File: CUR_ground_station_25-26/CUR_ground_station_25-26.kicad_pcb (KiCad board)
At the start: 4 copper layers, 74 x 51 mm, 82 parts, among them J1 Conn_01x02, J2 UJ20-C-H-G-SMT-P16-TR, J3 Conn_Coaxial_Small, J4 Conn_01x04_Pin, Q1 NTR4003N, Q2 NTR4003N, SW1 PTS815SJM250SMTRLFS, SW2 PTS815SJM250SMTRLFS, SW3 PTS815SJM250SMTRLFS, SW4 PTS815SJM250SMTRLFS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

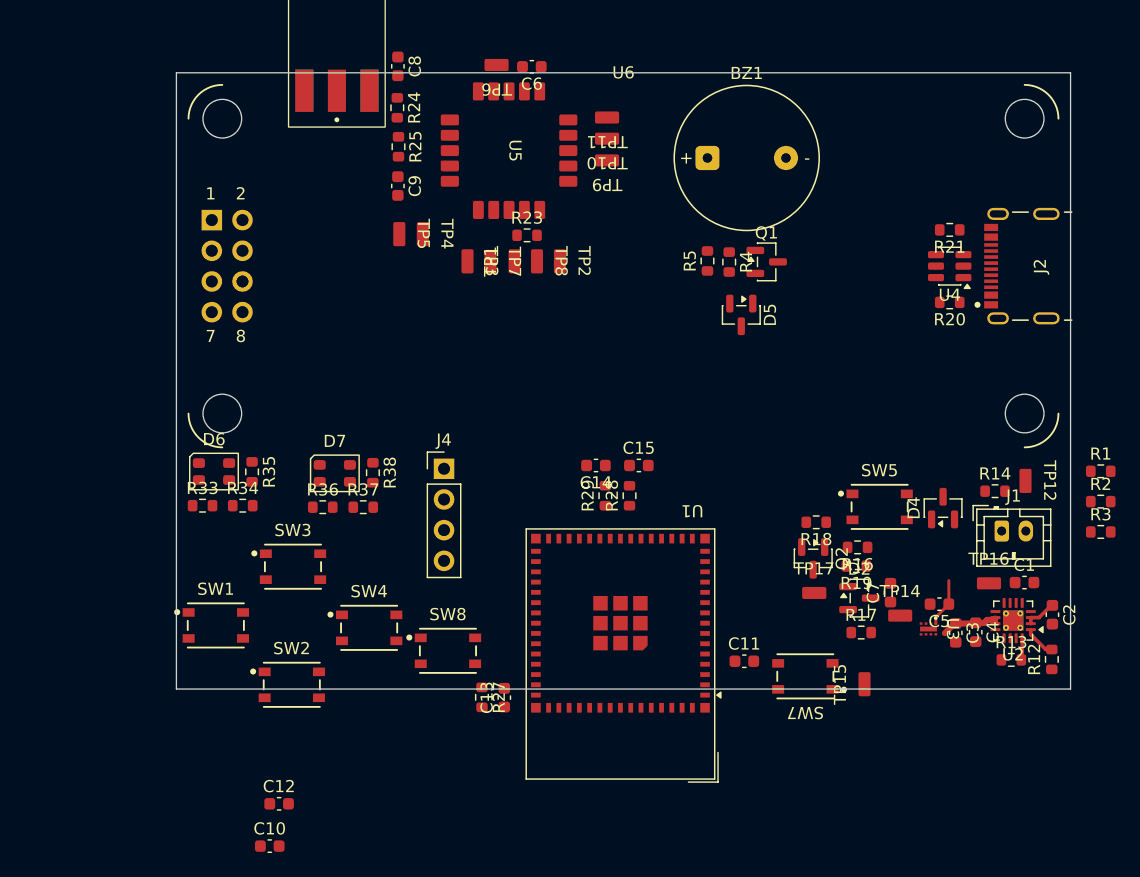
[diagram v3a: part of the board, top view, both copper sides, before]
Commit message: Add mounting holes
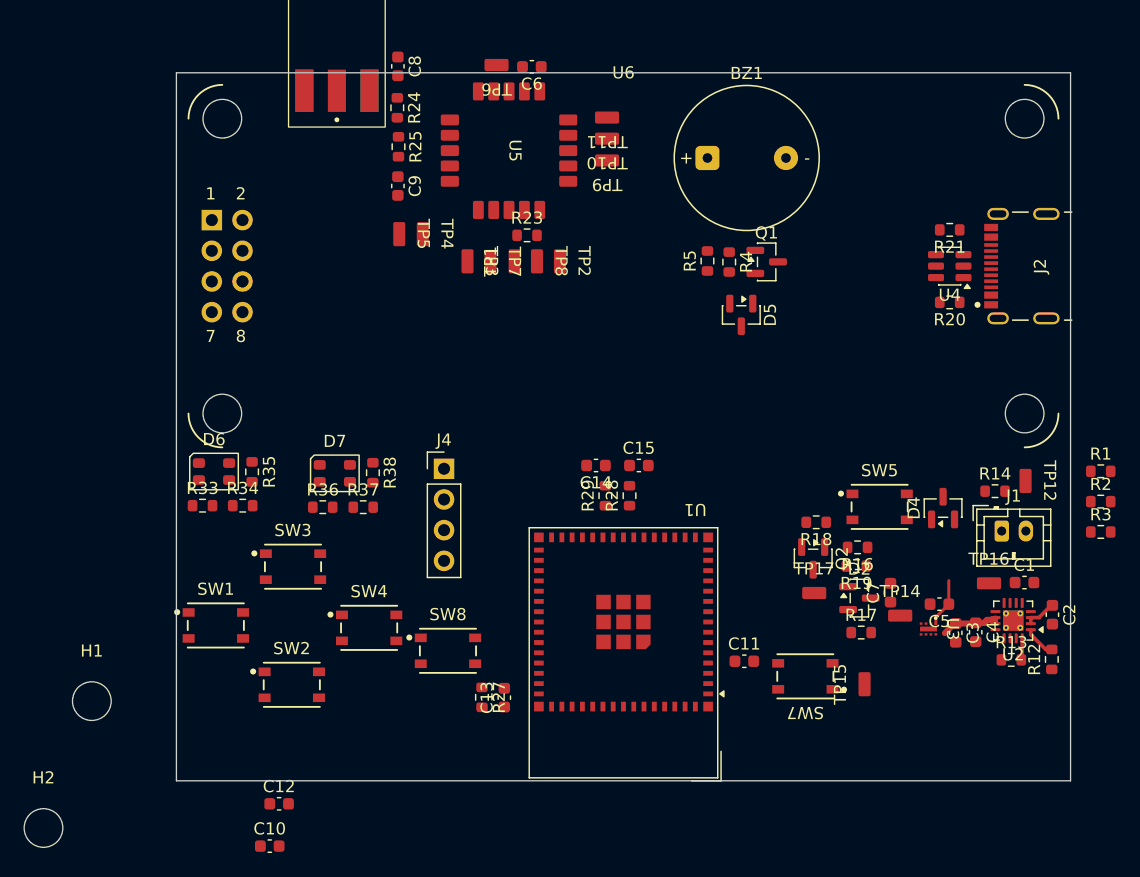
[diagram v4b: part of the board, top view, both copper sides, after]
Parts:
- added H1: MountingHole, MountingHole:MountingHole_3.2mm_M3, F.Cu at (41.5, 102.0)
- added H2: MountingHole, MountingHole:MountingHole_3.2mm_M3, F.Cu at (37.5, 112.5)
- moved U1 0.27 mm to (85.5, 98.0)
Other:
- board size 74 x 51 mm -> 74 x 58.6 mm
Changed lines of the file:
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@@
 		)
 	)
+	(footprint "MountingHole:MountingHole_3.2mm_M3"
+		(layer "F.Cu")
+		(at 37.5 112.5)
+		(descr "Mounting Hole 3.2mm, M3, no annular, generated by kicad-footprint-generator mountinghole.py")
+		(tags "mountinghole M3")
+		(property "Reference" "H2"
+			(at 0 -4.15 0)
+			(layer "F.SilkS")
+			(effects
+				(font
+					(size 1 1)
+					(thickness 0.15)
+				)
+			)
+		)
+		(property "Value" "MountingHole"
+			(at 0 4.15 0)
+			(layer "F.Fab")
+			(effects
+				(font
+					(size 1 1)
+					(thickness 0.15)
+				)
+			)
+		)
+		(property "Datasheet" "~"
+			(at 0 0 0)
+			(layer "F.Fab")
+			(hide yes)
+			(effects
+				(font
+					(size 1.27 1.27)
+					(thickness 0.15)
+				)
+			)
+		)
+		(property "Description" "Mounting Hole without connection"
+			(at 0 0 0)
+			(layer "F.Fab")
+			(hide yes)
+			(effects
+				(font
+					(size 1.27 1.27)
+					(thickness 0.15)
+				)
+			)
+		)
+		(property ki_fp_filters "MountingHole*")
+		(sheetname "/")
+		(sheetfile "CUR_ground_station_25-26.kicad_sch")
+		(attr exclude_from_pos_files exclude_from_bom)
+		(fp_circle
+			(center 0 0)
+			(end 3.2 0)
+			(stroke
+				(width 0.15)
+				(type solid)
+			)
+			(fill no)
+			(layer "Cmts.User")
+		)
+		(fp_circle
+			(center 0 0)
+			(end 3.45 0)
+			(stroke
+				(width 0.05)
+				(type solid)
+			)
+			(fill no)
+			(layer "F.CrtYd")
+		)
+		(fp_text user "${REFERENCE}"
+			(at 0 0 0)
+			(layer "F.Fab")
+			(effects
+				(font
+					(size 1 1)
+					(thickness 0.15)
+				)
+			)
+		)
+		(pad "" np_thru_hole circle
+			(at 0 0)
+			(size 3.2 3.2)
+			(drill 3.2)
+			(layers "*.Cu" "*.Mask")
+		)
+		(embedded_fonts no)
+	)
 	(footprint "Package_TO_SOT_SMD:SOT-23"
 		(layer "F.Cu")
@@
 		)
 	)
+	(footprint "MountingHole:MountingHole_3.2mm_M3"
+		(layer "F.Cu")
+		(at 41.5 102)
+		(descr "Mounting Hole 3.2mm, M3, no annular, generated by kicad-footprint-generator mountinghole.py")
+		(tags "mountinghole M3")
+		(property "Reference" "H1"
+			(at 0 -4.15 0)
+			(layer "F.SilkS")
+			(effects
+				(font
+					(size 1 1)
+					(thickness 0.15)
+				)
+			)
+		)
+		(property "Value" "MountingHole"
+			(at 0 4.15 0)
+			(layer "F.Fab")
+			(effects
+				(font
+					(size 1 1)
+					(thickness 0.15)
+				)
+			)
+		)
+		(property "Datasheet" "~"
+			(at 0 0 0)
+			(layer "F.Fab")
+			(hide yes)
+			(effects
+				(font
+					(size 1.27 1.27)
+					(thickness 0.15)
+				)
+			)
+		)
+		(property "Description" "Mounting Hole without connection"
+			(at 0 0 0)
+			(layer "F.Fab")
+			(hide yes)
+			(effects
+				(font
+					(size 1.27 1.27)
+					(thickness 0.15)
+				)
+			)
+		)
+		(property ki_fp_filters "MountingHole*")
+		(sheetname "/")
+		(sheetfile "CUR_ground_station_25-26.kicad_sch")
+		(attr exclude_from_pos_files exclude_from_bom)
+		(fp_circle
+			(center 0 0)
+			(end 3.2 0)
+			(stroke
+				(width 0.15)
+				(type solid)
+			)
+			(fill no)
+			(layer "Cmts.User")
+		)
+		(fp_circle
+			(center 0 0)
+			(end 3.45 0)
+			(stroke
+				(width 0.05)
+				(type solid)
+			)
+			(fill no)
+			(layer "F.CrtYd")
+		)
+		(fp_text user "${REFERENCE}"
+			(at 0 0 0)
+			(layer "F.Fab")
+			(effects
+				(font
+					(size 1 1)
+					(thickness 0.15)
+				)
+			)
+		)
+		(pad "" np_thru_hole circle
+			(at 0 0)
+			(size 3.2 3.2)
+			(drill 3.2)
+			(layers "*.Cu" "*.Mask")
+		)
+		(embedded_fonts no)
+	)
 	(footprint "Resistor_SMD:R_0603_1608Metric"
 		(layer "F.Cu")
@@
 	(footprint "RF_Module:ESP32-S2-MINI-1"
 		(layer "F.Cu")
-		(at 85.25 98.1 180)
+		(at 85.5 98 180)
 		(descr "2.4 GHz Wi-Fi and Bluetooth combo chip, external antenna, https://www.espressif.com/sites/default/files/documentation/esp32-s3-mini-1_mini-1u_datasheet_en.pdf")
 		(tags "2.4 GHz Wi-Fi Bluetooth external antenna espressif  20*15.4mm")
@@
 			(polygon
 				(pts
-					(xy 62.55 103.35) (xy 107.95 103.35) (xy 107.95 122.85) (xy 62.55 122.85)
+					(xy 62.8 103.25) (xy 108.2 103.25) (xy 108.2 122.75) (xy 62.8 122.75)
 				)
 			)
@@
 	(gr_rect
 		(start 48.5 50)
-		(end 122.5 101)
+		(end 122.5 108.595342)
 		(stroke
 			(width 0.05)

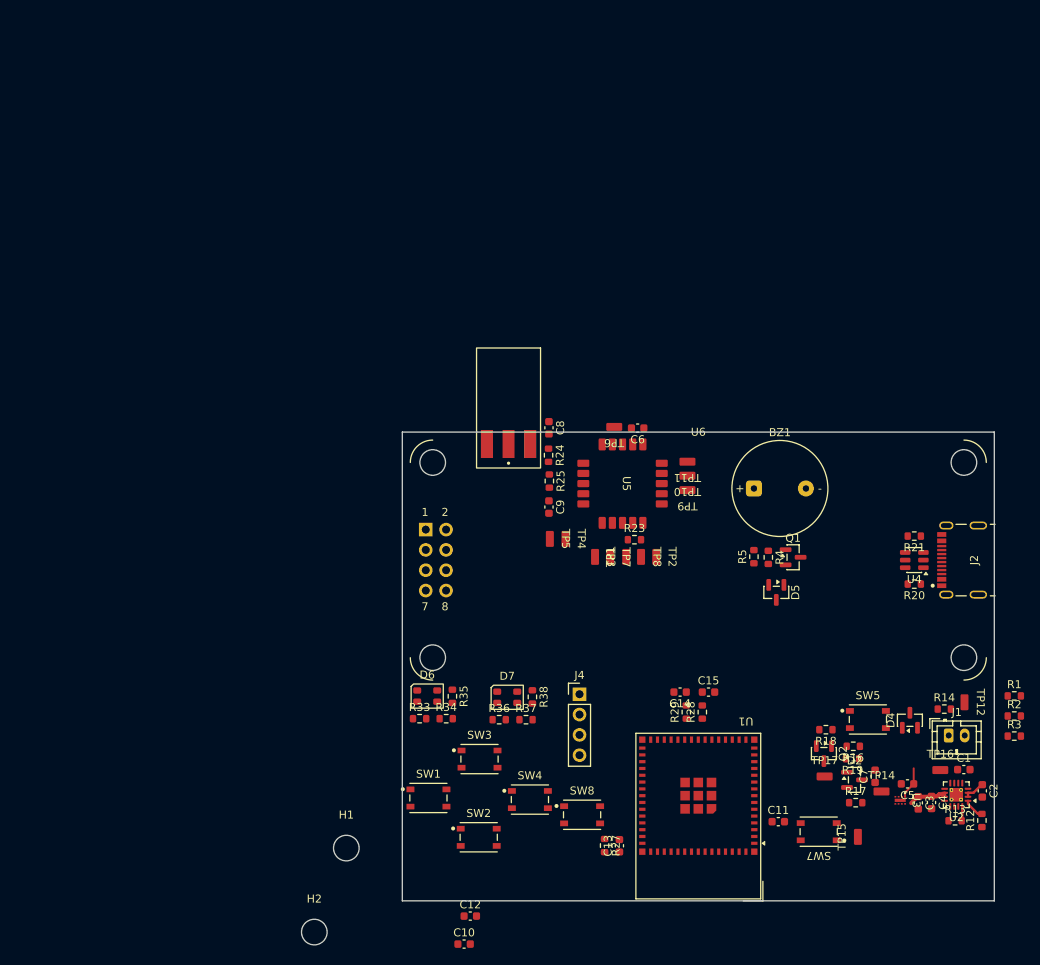
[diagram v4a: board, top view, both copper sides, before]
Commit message: switched battery connector, put mounting holes in place
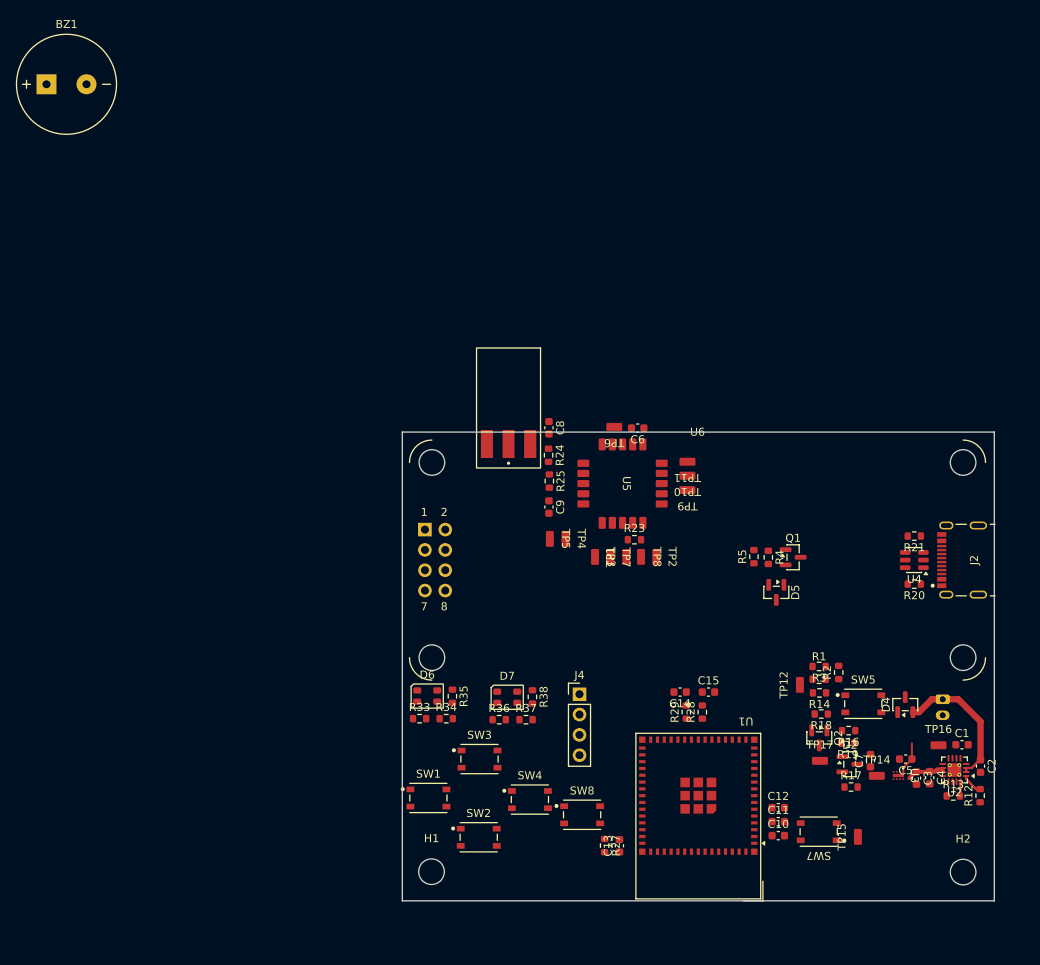
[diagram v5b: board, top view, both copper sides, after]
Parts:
- BZ1: footprint Buzzer_SameSky:Buzzer_SameSky_CEM-1203_42 -> Buzzer_SameSky:Buzzer_SameSky_CPT-1207-3TH
- J1: footprint Connector_JST:JST_PH_B2B-PH-K_1x02_P2.00mm_Vertical -> Connector_JST:JST_PH_S2B-PH-K_1x02_P2.00mm_Horizontal; moved to B.Cu
- moved BZ1 102.5 mm to (6.53, 6.53)
- moved H2 81.4 mm to (118.6, 105.0)
- moved C10 41.5 mm to (95.5, 100.5)
- moved C12 40.8 mm to (95.5, 97.0)
- moved R3 25.9 mm to (100.6, 79.3), turned to 180 degrees
- moved R1 24.5 mm to (100.6, 80.9)
- moved R2 22.6 mm to (103.0, 80.0), turned to 90 degrees
- moved TP12 20.7 mm to (98.2, 81.6), turned to 90 degrees
- moved R14 15.7 mm to (100.7, 82.6), turned to 180 degrees
- moved H1 11.1 mm to (52.1, 105.0)
- moved J1 4.59 mm to (116.0, 83.4), turned to -90 degrees
- moved C1 3.11 mm to (118.5, 89.1)
- moved R13 3.11 mm to (117.4, 95.5)
- moved C2 3.11 mm to (120.8, 91.7)
- moved C3 3.11 mm to (112.8, 93.2)
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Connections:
- U1 pad 7: /MCU/BATT_VSENSE -> /MCU/PWR_BTN
- U1 pad 9: /MCU/PWR_BTN -> /MCU/BATT_VSENSE
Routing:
- net +BATT: track 2.78 -> 17.8 mm

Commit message: Started routing power
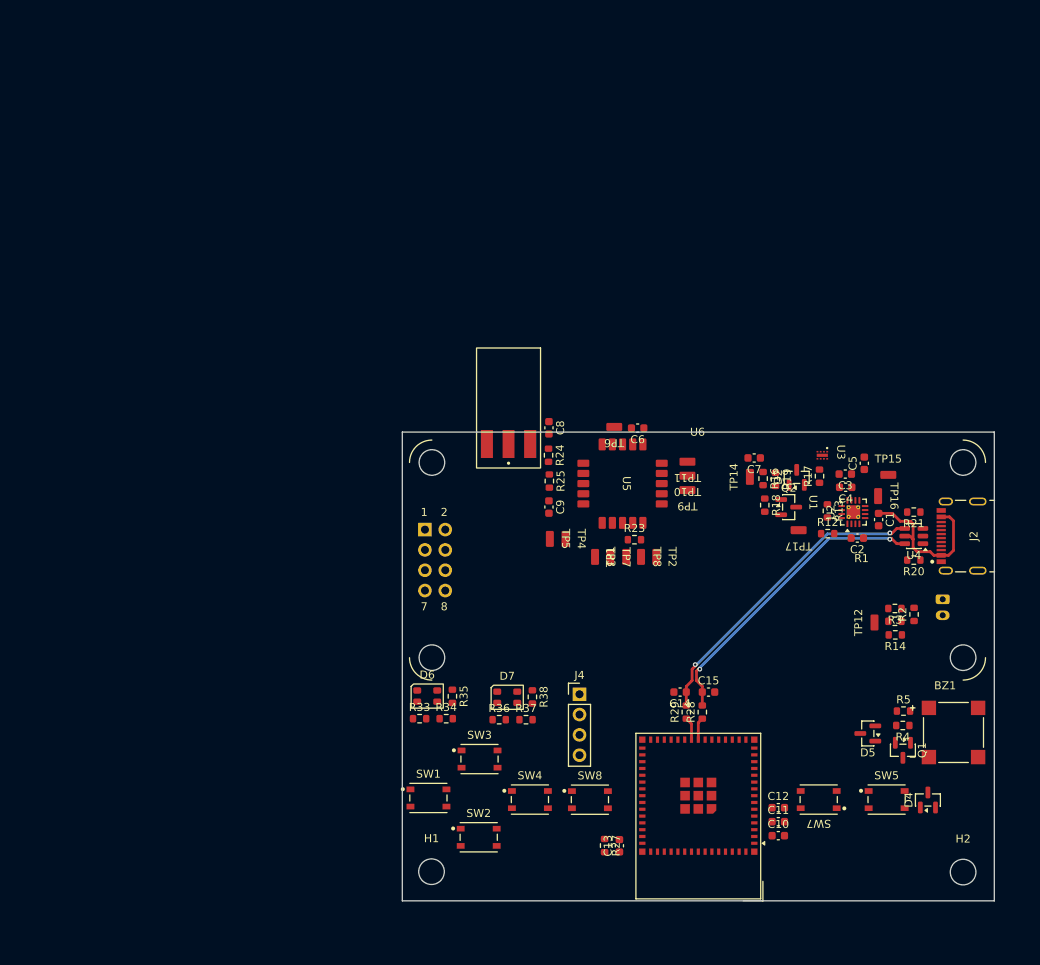
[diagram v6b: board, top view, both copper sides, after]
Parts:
- BZ1: footprint Buzzer_SameSky:Buzzer_SameSky_CPT-1207-3TH -> Buzzer_SameSky:XDCR_CMT-7525-03-SMT-TR
- moved BZ1 137.3 mm to (117.4, 87.5)
- moved TP15 45.4 mm to (109.3, 55.4), turned to 0 degrees
- moved U3 41.1 mm to (101.0, 52.9)
- moved TP14 40.6 mm to (92.0, 55.6), turned to 90 degrees
- moved C7 40.5 mm to (92.5, 53.2), turned to 180 degrees
- moved R17 39.1 mm to (100.6, 55.5), turned to 90 degrees
- moved C3 39.0 mm to (103.9, 55.2), turned to 180 degrees
- moved R13 39.0 mm to (101.6, 59.8), turned to -90 degrees
- moved R12 37.9 mm to (101.7, 62.7), turned to 0 degrees
- moved C4 37.8 mm to (103.9, 56.9), turned to 180 degrees
- moved C5 37.3 mm to (106.2, 53.9), turned to 90 degrees
- moved D2 36.5 mm to (97.8, 55.7), turned to 90 degrees
- moved U2 34.6 mm to (104.9, 60.0), turned to 90 degrees
- moved R19 34.2 mm to (95.1, 55.9), turned to -90 degrees
- moved R16 33.3 mm to (93.6, 55.8), turned to -90 degrees
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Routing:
- net /MCU/USB_D+: track 0.00 -> 38.9 mm, vias 0 -> 2
- net /MCU/USB_D-: track 0.00 -> 38.0 mm, vias 0 -> 2
- net VBUS: track 0.00 -> 20.2 mm
- net +BATT: track 17.8 -> 0.17 mm
- net IN: track 4.98 -> 0.17 mm
- net +3V3: track 4.01 -> 0.00 mm
- net Net-(U1-USB_D+): track 0.00 -> 2.89 mm
- net Net-(U1-USB_D-): track 0.00 -> 2.83 mm
- net Net-(U2-TS): track 2.65 -> 0.00 mm
- net Net-(U2-ISET): track 1.82 -> 0.11 mm
